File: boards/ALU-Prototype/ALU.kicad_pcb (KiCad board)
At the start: 2 copper layers, 50.2 x 45.7 mm, 58 parts, among them U1 7400, U10 7400, U11 7400, U12 7400, U13 7400, U14 7400, U15 7400, U16 7400, U2 7400, U3 7400, U4 7400, U5 7400, U6 7400, U7 7400, U8 7400, U9 7400

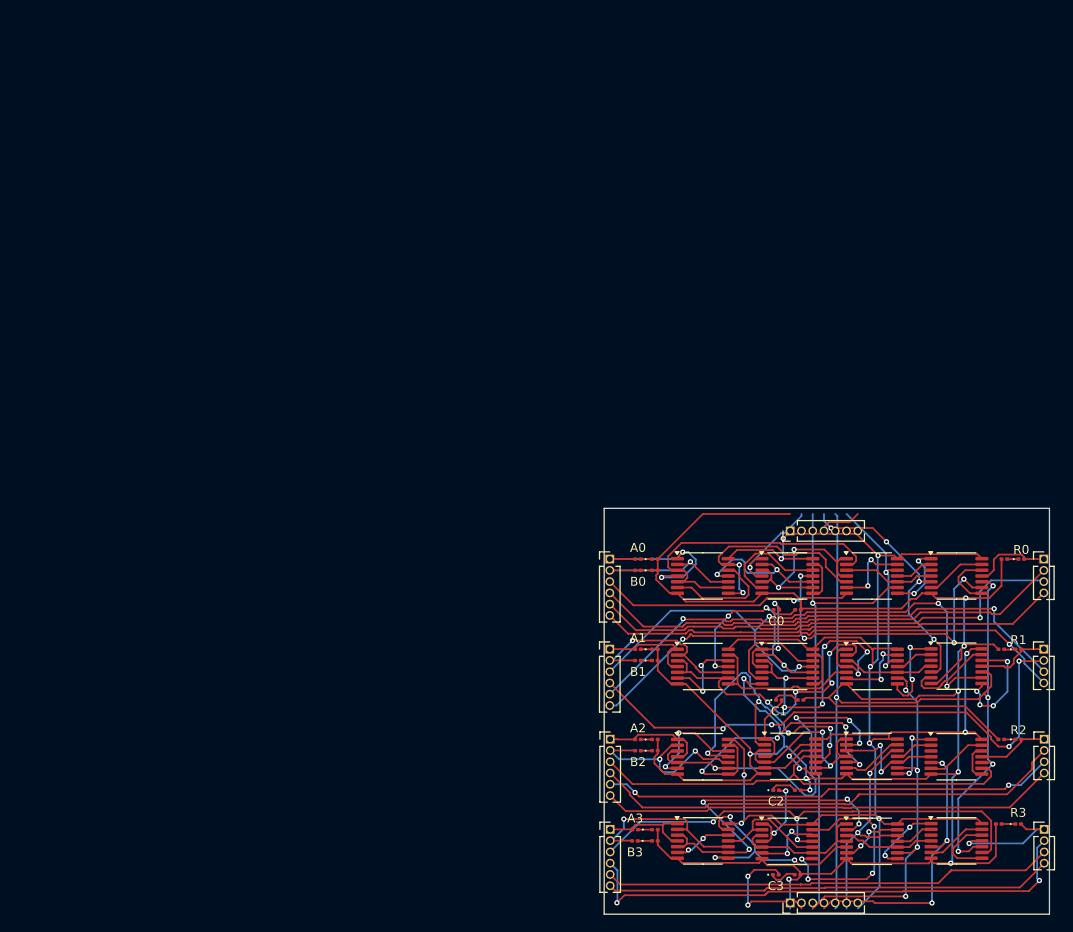
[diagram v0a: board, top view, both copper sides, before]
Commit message: pin headers (2*17 and 2*8)
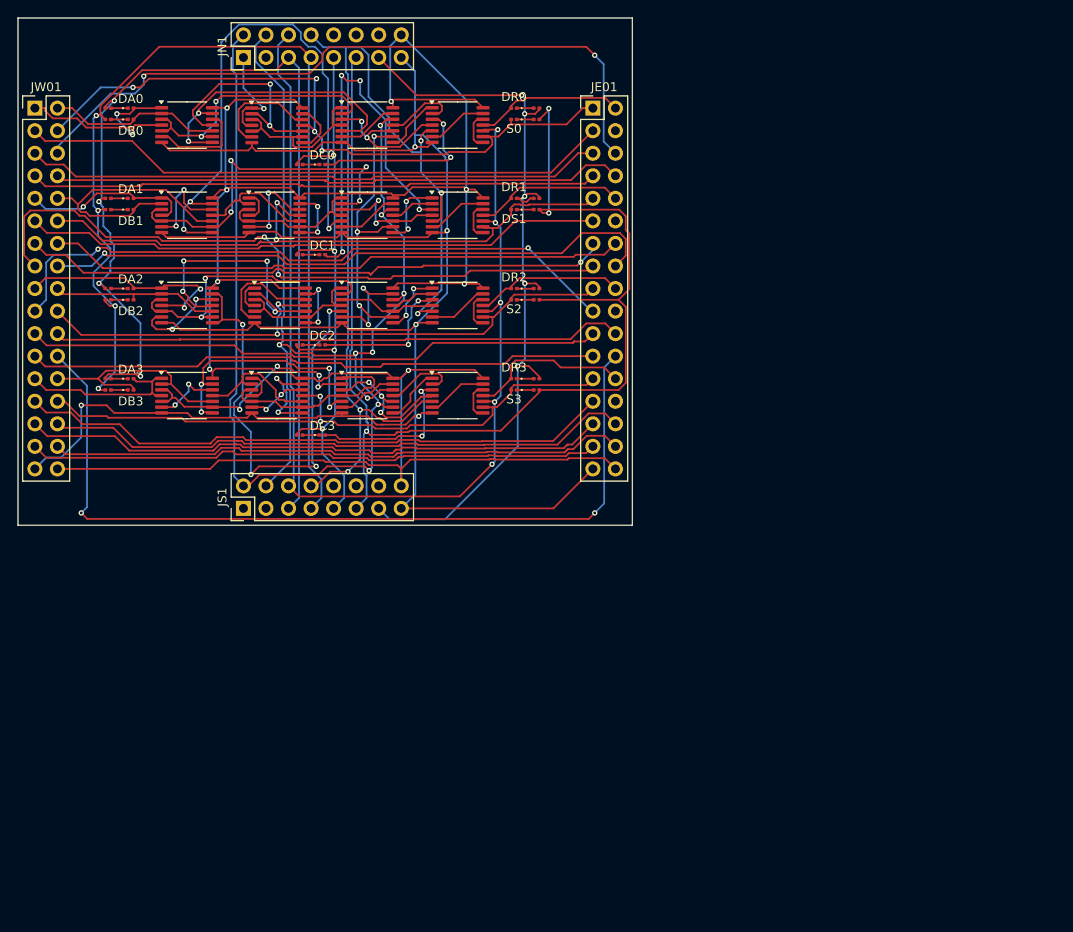
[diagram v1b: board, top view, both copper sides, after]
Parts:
- removed A0, A1, A2, A3, B0, B1, B2, B3, C0, C1, C2, C3, R0, R1, R2, R3: LED, LED_SMD:LED_0201_0603Metric
- removed JE0, JE1, JE2, JE3: Conn_01x04_Pin, Connector_PinHeader_1.27mm:PinHeader_1x04_P1.27mm_Vertical
- removed JN0, JS0: Conn_01x07_Pin, Connector_PinHeader_1.27mm:PinHeader_1x07_P1.27mm_Vertical
- removed JW0, JW1, JW2, JW3: Conn_01x06_Pin, Connector_PinHeader_1.27mm:PinHeader_1x06_P1.27mm_Vertical
- removed U1, U10, U15, U16, U2, U3, U4, U5, U6, U7, U8, U9: 7400, Package_SO:TSSOP-14_4.4x5mm_P0.65mm
- added DA0: LED, LED_SMD:LED_0201_0603Metric, F.Cu at (95.2, 48.9)
- added DA1: LED, LED_SMD:LED_0201_0603Metric, F.Cu at (95.2, 59.1)
- added DA2: LED, LED_SMD:LED_0201_0603Metric, F.Cu at (95.2, 69.2)
- added DA3: LED, LED_SMD:LED_0201_0603Metric, F.Cu at (95.2, 79.4)
- added DB0: LED, LED_SMD:LED_0201_0603Metric, F.Cu at (95.2, 50.2)
- added DB1: LED, LED_SMD:LED_0201_0603Metric, F.Cu at (95.2, 60.3)
- added DB2: LED, LED_SMD:LED_0201_0603Metric, F.Cu at (95.2, 70.5)
- added DB3: LED, LED_SMD:LED_0201_0603Metric, F.Cu at (95.2, 80.6)
- added DC0: LED, LED_SMD:LED_0201_0603Metric, F.Cu at (116.8, 55.2)
- added DC1: LED, LED_SMD:LED_0201_0603Metric, F.Cu at (116.8, 65.4)
- added DC2: LED, LED_SMD:LED_0201_0603Metric, F.Cu at (116.8, 75.6)
- added DC3: LED, LED_SMD:LED_0201_0603Metric, F.Cu at (116.8, 85.7)
- added DR0: LED, LED_SMD:LED_0201_0603Metric, F.Cu at (138.4, 48.9)
- added DR1: LED, LED_SMD:LED_0201_0603Metric, F.Cu at (138.4, 59.1)
- added DR2: LED, LED_SMD:LED_0201_0603Metric, F.Cu at (138.4, 69.2)
- added DR3: LED, LED_SMD:LED_0201_0603Metric, F.Cu at (138.4, 79.4)
- added DS1: LED, LED_SMD:LED_0201_0603Metric, F.Cu at (138.4, 60.3)
- added JE01: Conn_02x17_Odd_Even, Connector_PinHeader_2.54mm:PinHeader_2x17_P2.54mm_Vertical, F.Cu at (147.3, 48.9)
- added JN1: Conn_02x08_Odd_Even, Connector_PinHeader_2.54mm:PinHeader_2x08_P2.54mm_Vertical, F.Cu at (108.0, 43.2)
- added JS1: Conn_02x08_Odd_Even, Connector_PinHeader_2.54mm:PinHeader_2x08_P2.54mm_Vertical, F.Cu at (108.0, 94.0)
- added JW01: Conn_02x17_Odd_Even, Connector_PinHeader_2.54mm:PinHeader_2x17_P2.54mm_Vertical, F.Cu at (84.5, 48.9)
- added RS0: R, Resistor_SMD:R_0201_0603Metric, F.Cu at (141.0, 50.2)
- added RS1: R, Resistor_SMD:R_0201_0603Metric, F.Cu at (141.0, 60.3)
- added RS2: R, Resistor_SMD:R_0201_0603Metric, F.Cu at (141.0, 70.5)
- added RS3: R, Resistor_SMD:R_0201_0603Metric, F.Cu at (141.0, 80.6)
- added S0: LED, LED_SMD:LED_0201_0603Metric, F.Cu at (138.4, 50.2)
- added S2: LED, LED_SMD:LED_0201_0603Metric, F.Cu at (138.4, 70.5)
- added S3: LED, LED_SMD:LED_0201_0603Metric, F.Cu at (138.4, 80.6)
- added U01: 7400, Package_SO:TSSOP-14_4.4x5mm_P0.65mm, F.Cu at (101.6, 50.8)
- added U02: 7400, Package_SO:TSSOP-14_4.4x5mm_P0.65mm, F.Cu at (111.8, 50.8)
- added U03: 7400, Package_SO:TSSOP-14_4.4x5mm_P0.65mm, F.Cu at (121.9, 50.8)
- added U04: 7400, Package_SO:TSSOP-14_4.4x5mm_P0.65mm, F.Cu at (132.1, 50.8)
- added U21: 7400, Package_SO:TSSOP-14_4.4x5mm_P0.65mm, F.Cu at (101.6, 71.1)
- added U22: 7400, Package_SO:TSSOP-14_4.4x5mm_P0.65mm, F.Cu at (112.1, 71.1)
- added U23: 7400, Package_SO:TSSOP-14_4.4x5mm_P0.65mm, F.Cu at (121.9, 71.1)
- added U24: 7400, Package_SO:TSSOP-14_4.4x5mm_P0.65mm, F.Cu at (132.1, 71.1)
- added U31: 7400, Package_SO:TSSOP-14_4.4x5mm_P0.65mm, F.Cu at (101.6, 81.3)
- added U32: 7400, Package_SO:TSSOP-14_4.4x5mm_P0.65mm, F.Cu at (111.8, 81.3)
- added U33: 7400, Package_SO:TSSOP-14_4.4x5mm_P0.65mm, F.Cu at (121.9, 81.3)
- added U34: 7400, Package_SO:TSSOP-14_4.4x5mm_P0.65mm, F.Cu at (132.1, 81.3)
- moved U11 98.3 mm to (101.6, 61.0)
- moved U12 98.1 mm to (111.4, 61.0)
- moved U13 80.0 mm to (121.9, 61.0)
- moved RA1 79.8 mm to (92.7, 59.1), turned to 180 degrees
- moved RA2 79.8 mm to (92.7, 69.2), turned to 180 degrees
- moved RA3 79.8 mm to (92.7, 79.4), turned to 180 degrees
- moved RB0 79.8 mm to (92.7, 50.2), turned to 180 degrees
- moved RB1 79.8 mm to (92.7, 60.3), turned to 180 degrees
- moved RB2 79.8 mm to (92.7, 70.5), turned to 180 degrees
- moved RB3 79.8 mm to (92.7, 80.6), turned to 180 degrees
- moved RA0 79.8 mm to (92.7, 48.9), turned to 180 degrees
- moved U14 79.7 mm to (132.1, 61.0)
- moved RC1 75.5 mm to (114.3, 65.4), turned to 180 degrees
- moved RC0 75.3 mm to (114.3, 55.2), turned to 180 degrees
- moved RC2 75.3 mm to (114.3, 75.6), turned to 180 degrees
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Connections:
- RA0 pad 2: GND -> GNDA
- RA1 pad 2: GND -> GNDA
- RA2 pad 2: GND -> GNDA
- RA3 pad 2: GND -> GNDA
- RB0 pad 2: GND -> GNDB
- RB1 pad 2: GND -> GNDB
- RB2 pad 2: GND -> GNDB
- RB3 pad 2: GND -> GNDB
- RC0 pad 2: GND -> GNDC
- RC1 pad 2: GND -> GNDC
- RC2 pad 2: GND -> GNDC
- RC3 pad 2: GND -> GNDC
- RR0 pad 2: GND -> GNDR
- RR1 pad 2: GND -> GNDR
- RR2 pad 2: GND -> GNDR
- RR3 pad 2: GND -> GNDR
- U11 pad 1: Net-(U10-Pad3) -> A1
- U11 pad 10: Net-(U11-Pad10) -> B1
- U11 pad 12: /ALUSlice2/SUB -> Net-(U11-Pad12)
- U11 pad 2: Net-(U11-Pad2) -> B1
- U11 pad 3: Net-(U11-Pad10) -> Net-(U11-Pad3)
- U11 pad 4: Net-(U10-Pad3) -> A1
- U11 pad 5: Net-(U11-Pad5) -> Net-(U11-Pad3)
- U11 pad 6: Net-(U11-Pad13) -> Net-(U11-Pad12)
- U11 pad 8: Net-(U11-Pad8) -> Net-(U11-Pad13)
- U11 pad 9: /ALUSlice0/ADD -> Net-(U11-Pad3)
- U12 pad 1: Net-(U11-Pad8) -> /ALUSlice1/Cin
- U12 pad 10: /ALUSlice0/XOR -> Net-(U11-Pad11)
- U12 pad 11: RESULT2 -> S1
- U12 pad 3: /ALUSlice2/C -> Net-(U12-Pad3)
- U12 pad 4: Net-(U11-Pad10) -> /ALUSlice1/Cin
- U12 pad 5: /ALUSlice2/AND -> Net-(U12-Pad3)
- U12 pad 6: Net-(U12-Pad13) -> Net-(U12-Pad12)
- U12 pad 8: Net-(U12-Pad12) -> Net-(U12-Pad13)
- U12 pad 9: ADDOUT2 -> Net-(U12-Pad3)
- U13 pad 1: A3 -> Net-(U12-Pad3)
- U13 pad 10: B3 -> Net-(U13-Pad10)
- U13 pad 12: Net-(U13-Pad12) -> SUB
- U13 pad 2: B3 -> Net-(U11-Pad3)
- U13 pad 3: Net-(U13-Pad3) -> Net-(U13-Pad10)
- U13 pad 4: A3 -> Net-(U12-Pad3)
- U13 pad 5: Net-(U13-Pad3) -> Net-(U11-Pad13)
- U13 pad 6: Net-(U13-Pad12) -> Net-(U13-Pad13)
- U13 pad 8: Net-(U13-Pad13) -> Net-(U13-Pad8)
- U13 pad 9: Net-(U13-Pad3) -> ADD
- U14 pad 1: /ALUSlice2/Cout -> Net-(U13-Pad8)
- U14 pad 10: Net-(U13-Pad11) -> XOR
- U14 pad 11: ADDOUT3 -> R1
- U14 pad 3: Net-(U14-Pad3) -> /ALUSlice1/C
- U14 pad 4: /ALUSlice2/Cout -> Net-(U13-Pad10)
- U14 pad 5: Net-(U14-Pad3) -> AND
- U14 pad 6: Net-(U14-Pad12) -> Net-(U14-Pad13)
- U14 pad 8: Net-(U14-Pad13) -> Net-(U14-Pad12)
- U14 pad 9: Net-(U14-Pad3) -> S1
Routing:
- net GNDS: track 0.00 -> 138.7 mm, vias 0 -> 3
- net XOR: track 0.00 -> 122.7 mm, vias 0 -> 5
- net ADD: track 0.00 -> 120.1 mm, vias 0 -> 5
- net GNDB: track 0.00 -> 118.9 mm, vias 0 -> 4
- net GNDA: track 0.00 -> 117.0 mm, vias 0 -> 4
- net AND: track 0.00 -> 114.3 mm, vias 0 -> 5
- net SUB: track 0.00 -> 107.8 mm, vias 0 -> 7
- net /ALUSlice0/XOR: track 103.8 -> 0.00 mm, vias 5 -> 0
- net /ALUSlice0/ADD: track 98.0 -> 0.00 mm, vias 5 -> 0
- net PE2: track 0.00 -> 96.3 mm, vias 0 -> 2
- net GNDR: track 0.00 -> 86.9 mm, vias 0 -> 5
- net PD0: track 0.00 -> 79.3 mm, vias 0 -> 2
- net VDD: track 182.3 -> 260.7 mm, vias 10 -> 8
- net S0: track 0.00 -> 77.8 mm, vias 0 -> 4
- net PC1: track 0.00 -> 76.1 mm, vias 0 -> 2
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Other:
- board size 50.2 x 45.7 mm -> 69.2 x 57.2 mm
